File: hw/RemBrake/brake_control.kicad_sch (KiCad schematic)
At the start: 38 parts, among them J7 Conn_01x07, J8 Conn_01x07, J9 Conn_01x03, Q6 BC337, Q7 BC847, U5 LM555xN, U6 BD5230G-TR

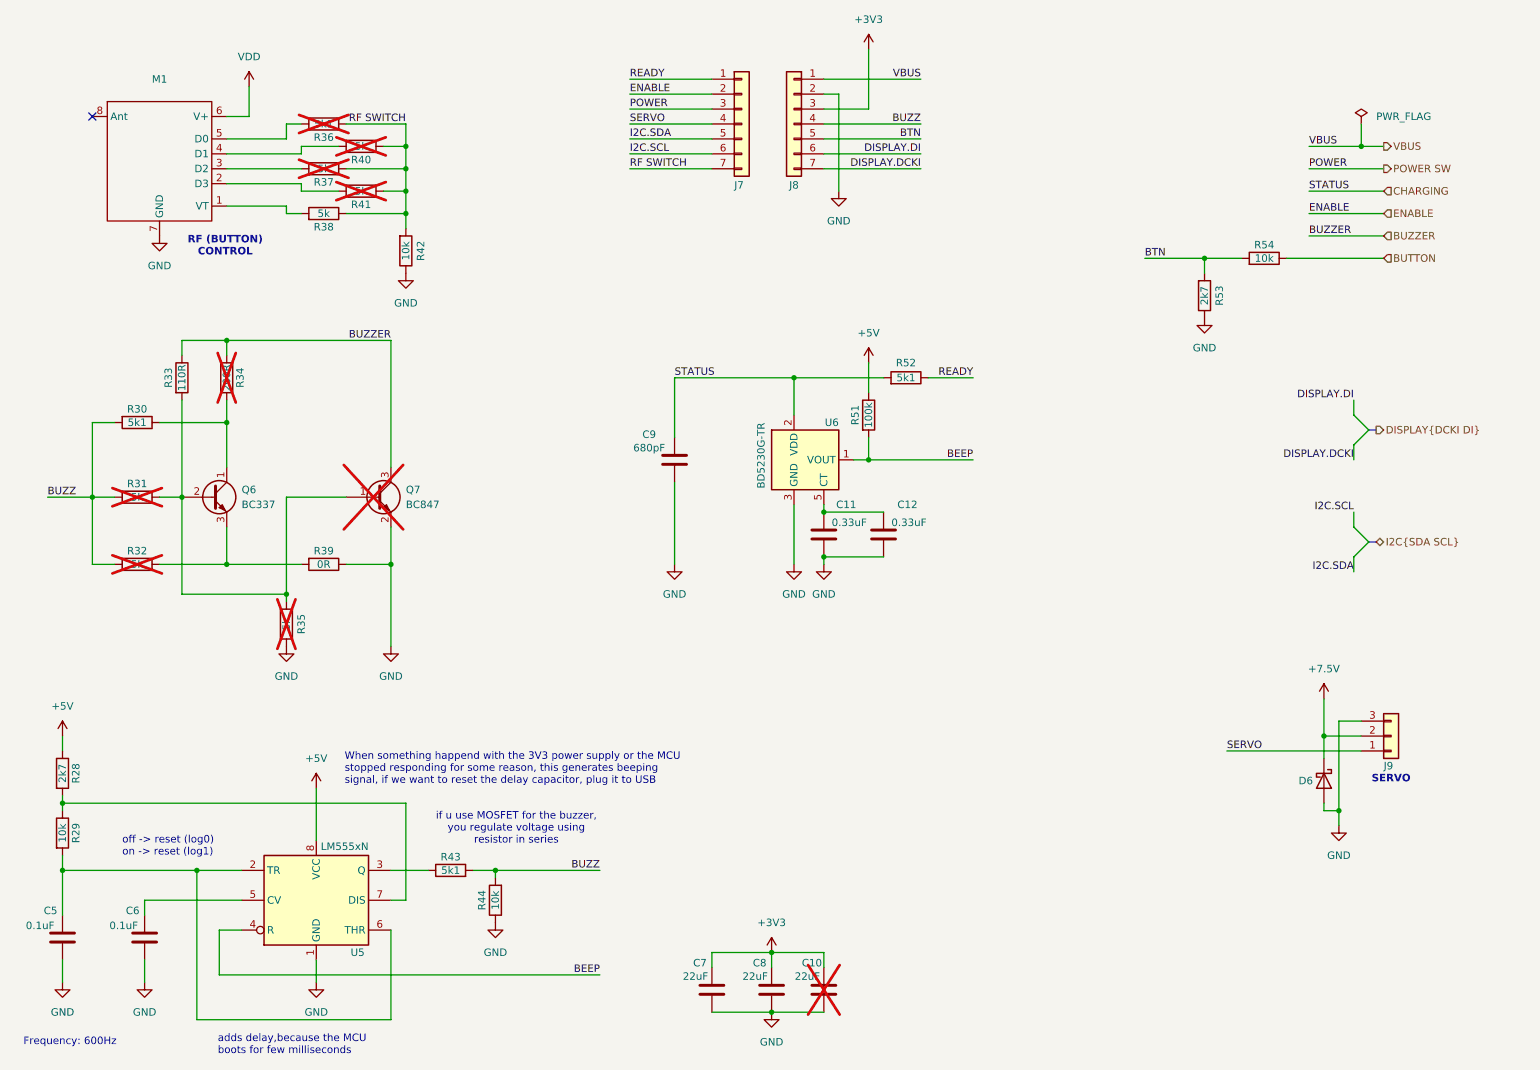
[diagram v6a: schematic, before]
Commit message: finished todos - prepared for routing
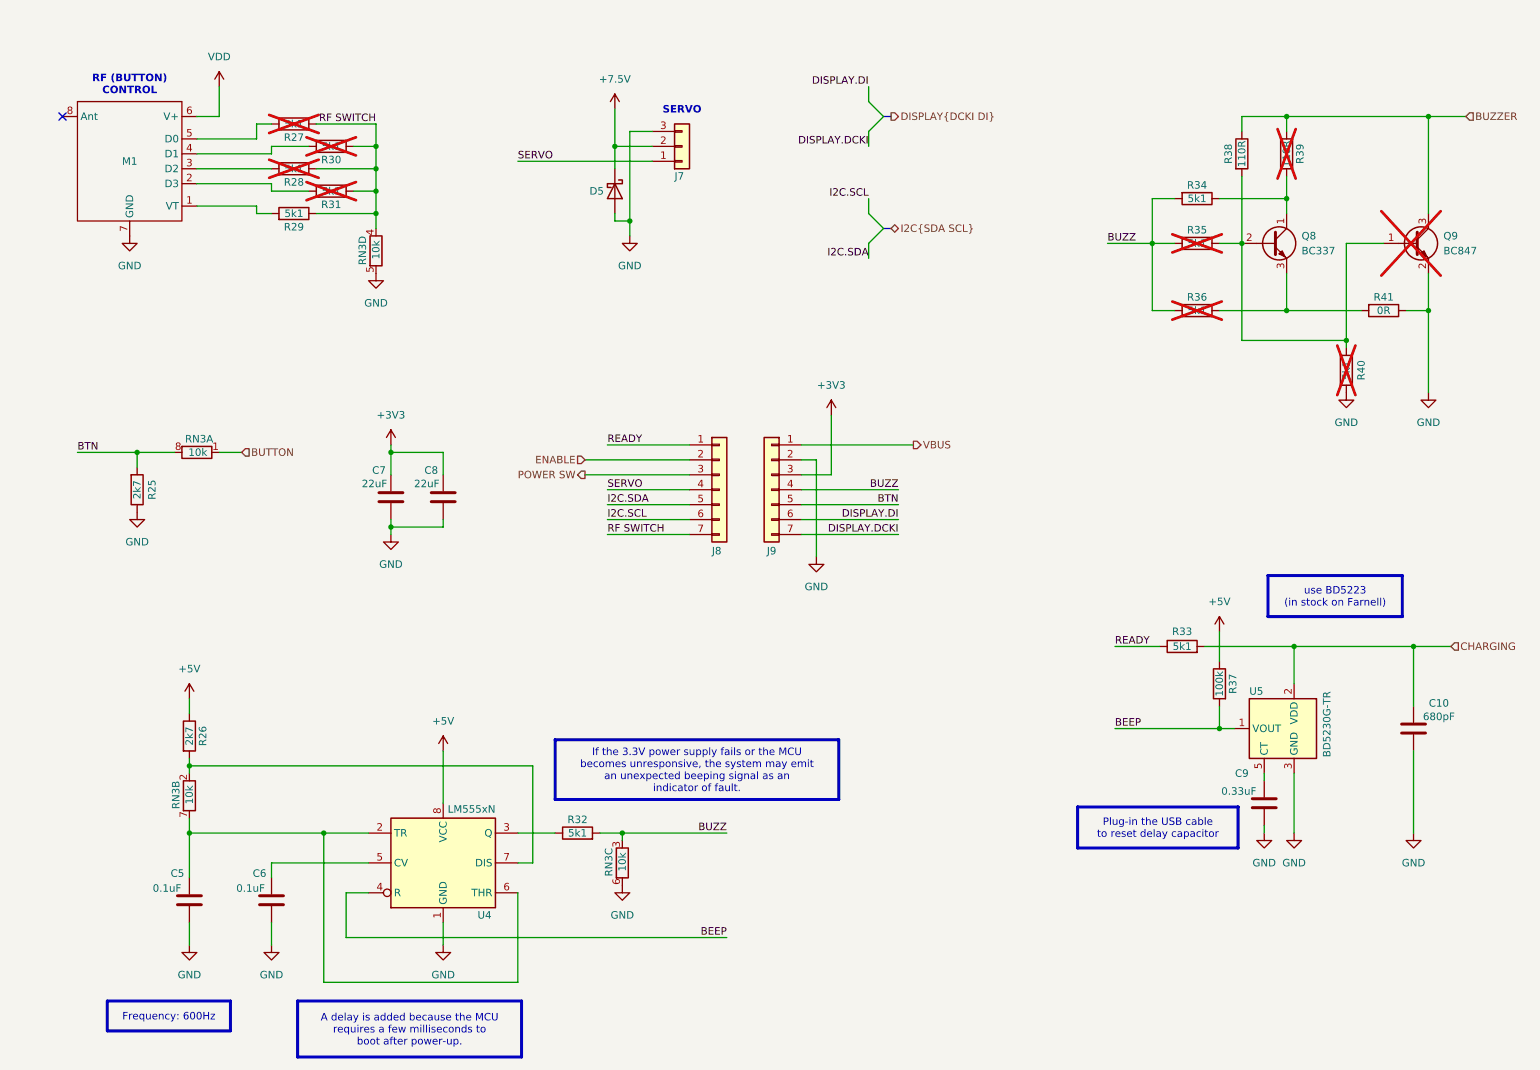
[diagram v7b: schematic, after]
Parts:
- removed C10: 22uF, Capacitor_SMD:C_0805_2012Metric_Pad1.18x1.45mm_HandSolder, symbol Device:C
- removed C12: 0.33uF, Capacitor_SMD:C_0805_2012Metric_Pad1.18x1.45mm_HandSolder, symbol Device:C
- removed R29, R42, R44, R54: 10k, Resistor_SMD:R_0805_2012Metric_Pad1.20x1.40mm_HandSolder, symbol Device:R
- added RN3: 10k, Resistor_SMD:R_Array_Convex_4x0603, symbol Device:R_Pack04_Split
- R28: renamed from R37; value 5k -> 5k1
- R29: renamed from R38; value 5k -> 5k1
- R30: renamed from R40; value 5k -> 5k1
- R31: renamed from R41; value 5k -> 5k1
- R35: renamed from R31; value 5k -> 5k1
- R36: renamed from R32; value 5k -> 5k1
- R39: renamed from R34; value 200R -> 110R
- R40: renamed from R35; value 5k -> 5k1
- U5: renamed from U6; footprint Package_TO_SOT_SMD:SOT-23-6_Handsoldering -> Package_TO_SOT_SMD:SOT-23-5
- renumbered C9 to C10, C11 to C9, D6 to D5, J9 to J7, J7 to J8, J8 to J9, Q6 to Q8, Q7 to Q9, R53 to R25, R28 to R26, R36 to R27, R43 to R32, R52 to R33, R30 to R34, R51 to R37, R33 to R38, R39 to R41, U5 to U4
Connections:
- net BTN: now also RN3.8 (R1.2)
- net BUTTON: now also RN3.1 (R1.1)
- net BUZZ: now also RN3.3 (R3.1)
- net GND: now also RN3.5 (R4.2), RN3.6 (R3.2)
- net RF SWITCH: now also RN3.4 (R4.1)
- net at C5.1, U4.2 (TR), U4.6 (THR): now also RN3.7 (R2.2)
- net at R26.2, U4.7 (DIS): now also RN3.2 (R2.1)
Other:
- note removed: "Frequency: 600Hz"
- note removed: "When something happend with the 3V3 power supply or the MCU stopped responding for some reason, this generates beeping signal, if we want to reset the delay capacitor, plug it to USB"
- note removed: "adds delay,because the MCU boots for few milliseconds"
- note removed: "if u use MOSFET for the buzzer, you regulate voltage using resistor in series"
- note removed: "off -> reset (log0) on -> reset (log1)"
- moved on the sheet: C10, C5, C6, C7, C9, D5, J7, J8, J9, M1, Q8, R25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

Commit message: new routing version 3.0 with power mosfet swich for the charger and fixed problems with LED and buzzer reset delayed circuit
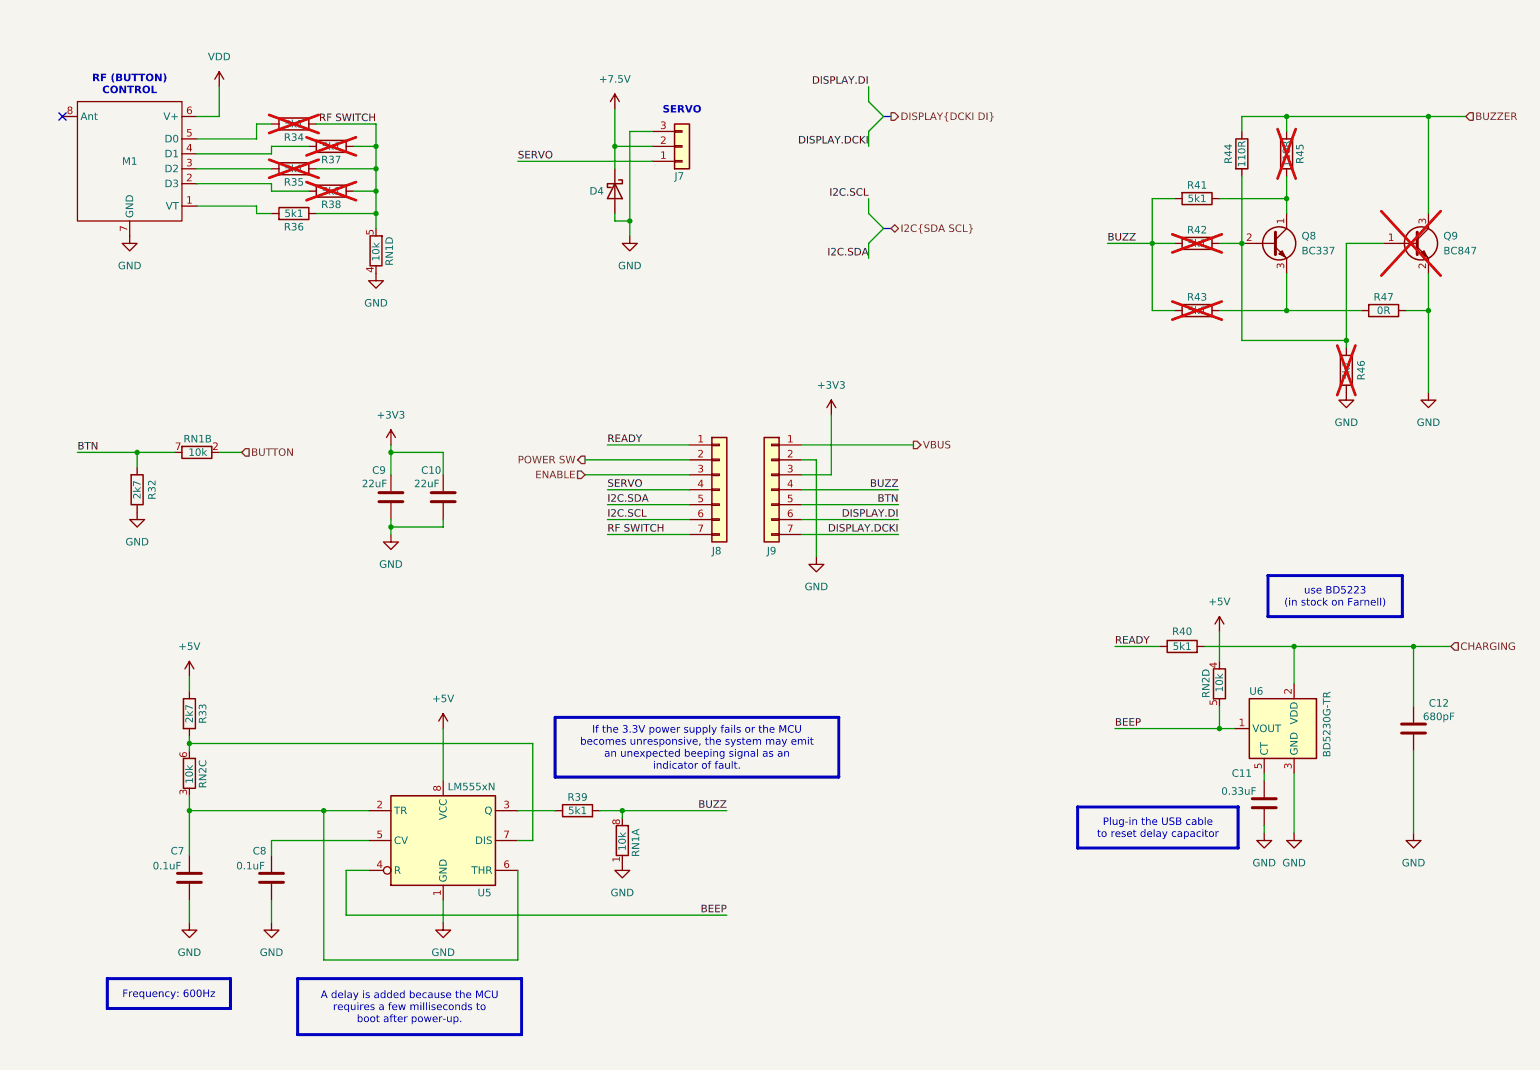
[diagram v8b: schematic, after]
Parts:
- removed R37: 100k, Resistor_SMD:R_0805_2012Metric_Pad1.20x1.40mm_HandSolder, symbol Device:R
- removed RN3: 10k, Resistor_SMD:R_Array_Convex_4x0603, symbol Device:R_Pack04_Split
- added RN1, RN2: 10k, Resistor_SMD:R_Array_Convex_4x0603, symbol Device:R_Pack04_Split
- renumbered C8 to C10, C9 to C11, C10 to C12, C5 to C7, C6 to C8, C7 to C9, D5 to D4, R25 to R32, R26 to R33, R27 to R34, R28 to R35, R29 to R36, R30 to R37, R31 to R38, R32 to R39, R33 to R40, R34 to R41, R35 to R42, R36 to R43, R38 to R44, R39 to R45, R40 to R46, R41 to R47, U4 to U5, U5 to U6
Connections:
- net +5V: now also RN2.4 (R4.1)
- net BEEP: now also RN2.5 (R4.2)
- net BTN: now also RN1.7 (R2.2)
- net BUTTON: now also RN1.2 (R2.1)
- net BUZZ: now also RN1.8 (R1.2)
- net ENABLE: now also J8.3 (Pin_3); no longer J8.2 (Pin_2)
- net GND: now also RN1.1 (R1.1), RN1.4 (R4.1)
- net POWER SW: now also J8.2 (Pin_2); no longer J8.3 (Pin_3)
- net RF SWITCH: now also RN1.5 (R4.2)
- net at C7.1, U5.2 (TR), U5.6 (THR): now also RN2.3 (R3.1)
- net at R33.2, U5.7 (DIS): now also RN2.6 (R3.2)
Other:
- moved on the sheet: C7, C8, R33, R39, U5
